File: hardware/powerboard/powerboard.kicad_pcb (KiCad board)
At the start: 2 copper layers, 45 x 30 mm, 45 parts, among them J1 BAT JST-PH 2P, J2 SERVO L, J3 SERVO R, J4 DISPLAY GC9A01, Q1 AO3401A, Q2 FS8205A, Q3 AO3401A, Q4 2N7002, Q5 AO3401A, SW1 EIN/AUS, U1 TP4054, U2 DW01A, U3 LM66100, U4 ESP32-C6-Zero

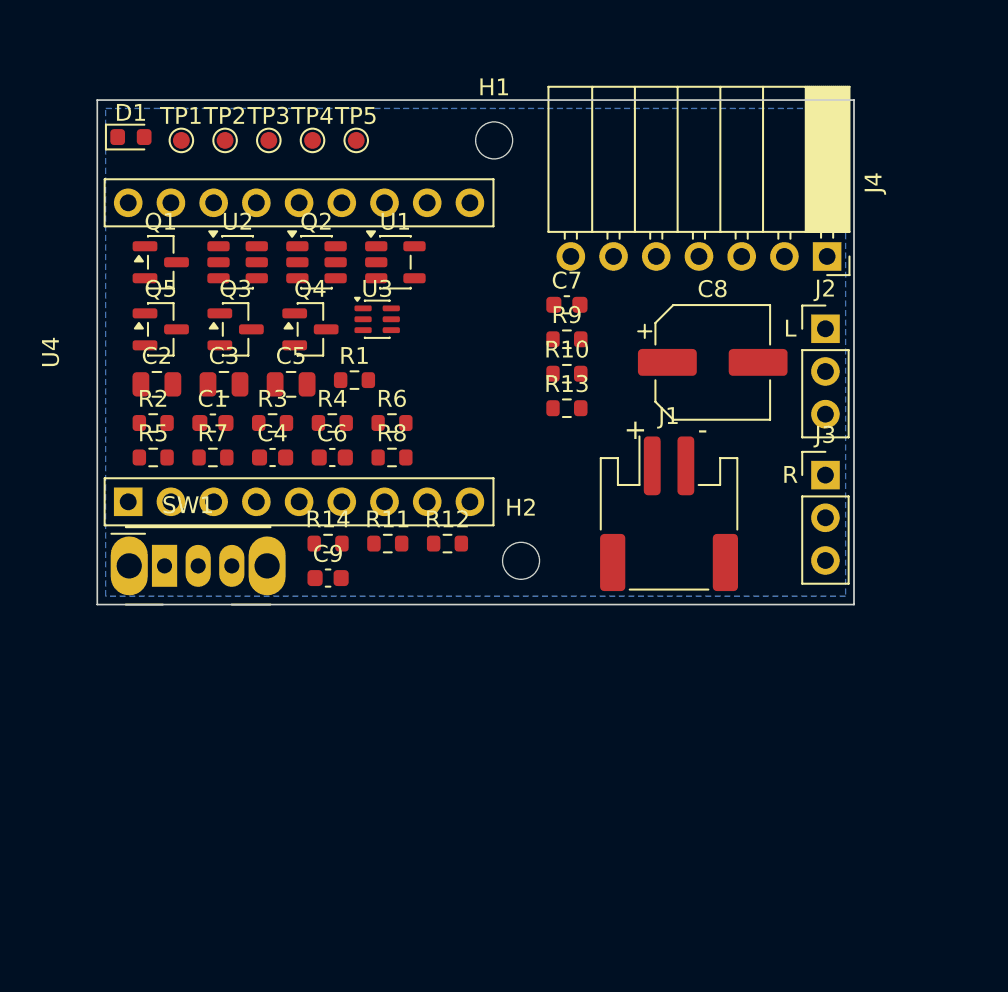
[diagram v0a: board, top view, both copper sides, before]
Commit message: Route the powerboard Rev 0.2 and add the files for a JLCPCB order
The board now has four 5 V servo ports through a TPS61023 boost, current
and voltage measurement with an INA226 on a Kelvin shunt, three analog and
two I2C ports, a THT cell connector and the outline of the shell. JLC basic
parts are used where they cost nothing in function.

The high current path (cell, reverse polarity FETs, shunt, boost, 5 V rail)
sits in one block at the front and is drawn with fixed, wide copper; the
autorouter only does signals and low current. Freerouting cannot reach pads
of parts at odd angles or next to slanted edges, so route.py rewrites the
DSN for it, tries several variants and keeps the best; maze.py closes what
is left. Labels on both sides and the KidsLab logo on the bottom.

Co-Authored-By: Claude Opus 5.5 <noreply@anthropic.com>
Claude-Session: https://claude.ai/code/session_01UqX4DjfVzW8YQJ4gc8FRQe
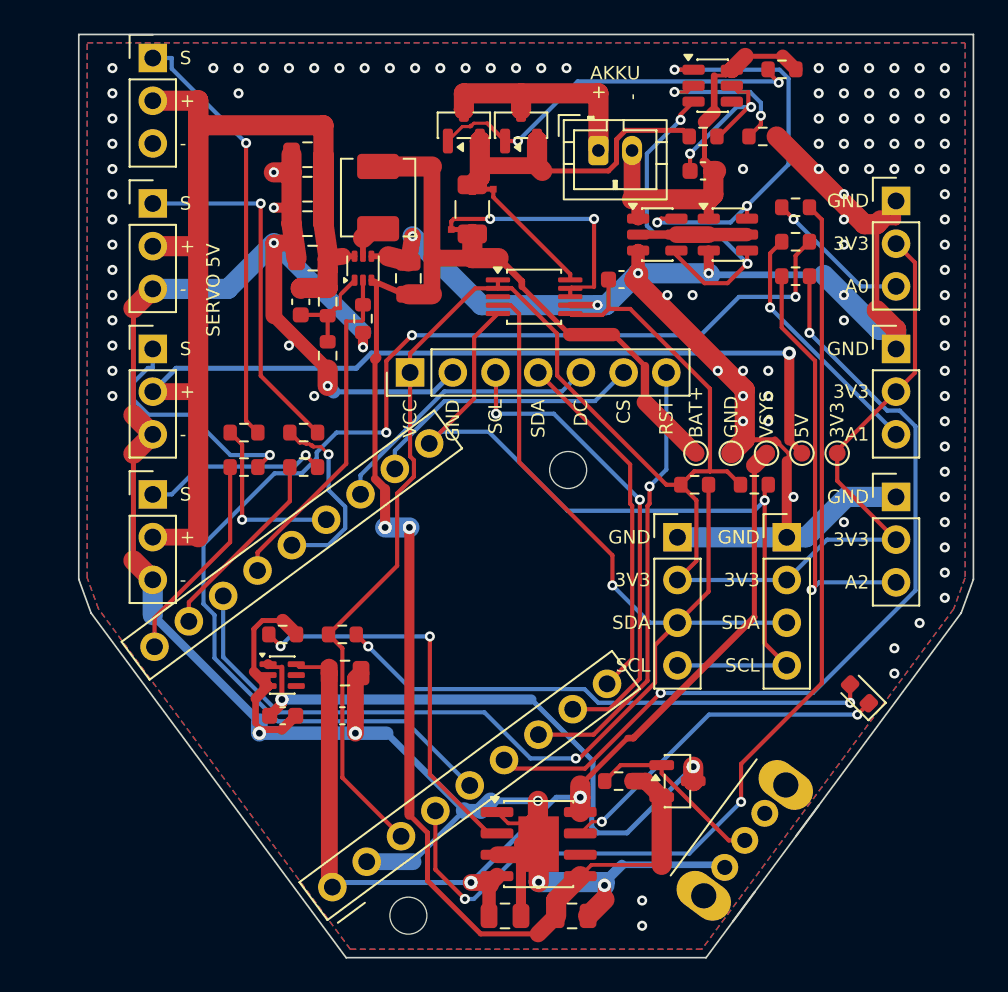
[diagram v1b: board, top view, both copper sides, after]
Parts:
- removed C8: 470u 10V, CP_Elec_6.3x7.7
- removed C9: 100n, C_0603_1608Metric
- removed Q3: AO3401A, SOT-23
- removed Q4: 2N7002, SOT-23
- removed R11, R12: 470k, R_0603_1608Metric
- removed R6: 10k, R_0603_1608Metric
- added C10: 22u, C_0805_2012Metric, F.Cu at (118.5, 110.6)
- added C11: 22u, C_0805_2012Metric, F.Cu at (112.8, 109.4)
- added C12: 22u, C_0805_2012Metric, F.Cu at (112.5, 107.3)
- added C13: 22u, C_0805_2012Metric, F.Cu at (112.5, 105.3)
- added C14: 22u, C_0805_2012Metric, F.Cu at (112.5, 103.2)
- added C15: 100n, C_0603_1608Metric, F.Cu at (131.2, 110.7)
- added J10: I2C 1, PinHeader_1x04_P2.54mm_Vertical, F.Cu at (134.5, 126.0)
- added J11: I2C 2, PinHeader_1x04_P2.54mm_Vertical, F.Cu at (141.0, 126.0)
- added J5: SERVO 3, PinHeader_1x03_P2.54mm_Vertical, F.Cu at (103.3, 114.8)
- added J6: SERVO 4, PinHeader_1x03_P2.54mm_Vertical, F.Cu at (103.3, 123.5)
- added J7: ANALOG A0, PinHeader_1x03_P2.54mm_Vertical, F.Cu at (147.5, 106.0)
- added J8: ANALOG A1, PinHeader_1x03_P2.54mm_Vertical, F.Cu at (147.5, 114.8)
- added J9: ANALOG A2, PinHeader_1x03_P2.54mm_Vertical, F.Cu at (147.5, 123.6)
- added L1: 1u, L_Sunlord_MWSA0402S, F.Cu at (116.7, 105.8)
- added LOGO1: KidsLab_Logo, KidsLab_Logo, B.Cu at (118.5, 105.5)
- added Q6: FS8205A, SOT-23-6, F.Cu at (137.5, 108.0)
- added Q7: AO3401A, SOT-23, F.Cu at (125.2, 101.5)
- added R15: 10m, R_1206_3216Metric_Kelvin, F.Cu at (122.3, 106.5)
- added R16: 220, R_0603_1608Metric, F.Cu at (108.7, 121.8)
- added R17: 220, R_0603_1608Metric, F.Cu at (112.3, 121.8)
- added R18: 1k, R_0603_1608Metric, F.Cu at (141.5, 106.4)
- added R19: 1k, R_0603_1608Metric, F.Cu at (141.5, 108.4)
- added R20: 1k, R_0603_1608Metric, F.Cu at (141.5, 110.5)
- added R21: 4.7k, R_0603_1608Metric, F.Cu at (135.5, 122.9)
- added R22: 4.7k, R_0603_1608Metric, F.Cu at (139.1, 122.9)
- added U5: INA226, TSSOP-10_3x3mm_P0.5mm, F.Cu at (126.0, 111.7)
- added U6: TPS61023, SOT-563, F.Cu at (115.8, 110.0)
- C7: value 47n -> 220p
- J1: footprint JST_PH_S2B-PH-SM4-TB_1x02-1MP_P2.00mm_Horizontal -> JST_PH_B2B-PH-K_1x02_P2.00mm_Vertical
- J2: value SERVO L -> SERVO 1
- J3: value SERVO R -> SERVO 2
- J4: footprint PinSocket_1x07_P2.54mm_Horizontal -> PinHeader_1x07_P2.54mm_Vertical
- R8: value 100k -> 750k
- R9: value 10k -> 100k
- SW1: footprint SW_Slide_SPDT_Angled_CK_OS102011MA1Q -> SW_Slide_SPDT_Angled_CK_OS102011MA1Q_Round
- TP4: value TP_VSERVO -> TP_V5_SERVO
- U1: value TP4054 -> TP4056; footprint SOT-23-5 -> SOIC-8-1EP_3.9x4.9mm_P1.27mm_EP2.41x3.3mm
- moved D1 54.5 mm to (145.3, 135.3), turned to 135 degrees
- moved J3 43.1 mm to (103.3, 106.2)
- moved J2 43.1 mm to (103.3, 97.5)
- moved Q5 40.8 mm to (134.5, 140.5)
- moved SW1 37.8 mm to (137.3, 145.6), turned to 53.4986 degrees
- moved C2 37.8 mm to (124.2, 148.5)
- moved C3 37.8 mm to (128.2, 148.5)
- moved R2 36.9 mm to (136.0, 102.2)
- moved TP1 35.8 mm to (135.6, 121.0)
- moved U1 35.6 mm to (126.2, 144.2)
- moved TP2 35.4 mm to (137.7, 121.0)
- moved TP3 35.0 mm to (139.8, 121.0)
- moved TP4 34.5 mm to (141.9, 121.0)
- moved TP5 34.1 mm to (144.0, 121.0)
- moved R3 33.8 mm to (139.6, 102.2)
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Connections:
- net /SERVO_L renamed /SERVO1
- net /SERVO_L_S renamed /SERVO1_S
- net /SERVO_R renamed /SERVO2
- net /SERVO_R_S renamed /SERVO2_S
- C7 pad 1: /SERVO_G -> /V5_SERVO
- C7 pad 2: /BAT+ -> /BOOST_FB
- J2 pad 2: /VSERVO -> /V5_SERVO
- J3 pad 2: /VSERVO -> /V5_SERVO
- Q1 pad 2: /BAT+ -> /BAT_CELL
- R2 pad 1: /BAT+ -> /BAT_CELL
- R8 pad 1: /SERVO_G -> /V5_SERVO
- R8 pad 2: /BAT+ -> /BOOST_FB
- R9 pad 1: /SERVO_G -> /BOOST_FB
- R9 pad 2: /Q4_D -> /GND
- TP4 pad 1: /VSERVO -> /V5_SERVO
- U1 pad 1: /CHRG_N -> /GND
- U1 pad 2: /GND -> /PROG
- U1 pad 3: /BAT+ -> /GND
- U1 pad 5: /PROG -> /BAT+
- U4 pad 10: (no net) -> /SERVO3
- U4 pad 11: (no net) -> /SERVO4
- U4 pad 12: (no net) -> /I2C_SDA
- U4 pad 13: (no net) -> /SERVO_EN
- U4 pad 18: (no net) -> /I2C_SCL
- U4 pad 4: /VBAT_SENSE -> /A0_IO
- U4 pad 5: /CHRG_IO -> /A1_IO
- U4 pad 6: /SERVO_EN -> /A2_IO
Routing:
- net /GND: track 0.00 -> 243.8 mm, vias 0 -> 115
- net /3V3: track 0.00 -> 120.5 mm
- net /V5_SERVO: track 0.00 -> 115.0 mm, vias 0 -> 1
- net /BAT+: track 0.00 -> 99.0 mm, vias 0 -> 2
- net /I2C_SDA: track 0.00 -> 78.0 mm, vias 0 -> 2
- net /A1_IO: track 0.00 -> 73.0 mm, vias 0 -> 3
- net /A0_IO: track 0.00 -> 62.4 mm, vias 0 -> 2
- net /VSYS: track 0.00 -> 61.9 mm, vias 0 -> 2
- net /A2_IO: track 0.00 -> 50.8 mm, vias 0 -> 2
- net /I2C_SCL: track 0.00 -> 49.7 mm, vias 0 -> 1
- net /BAT_SW: track 0.00 -> 36.7 mm, vias 0 -> 2
- net /LED_A: track 0.00 -> 32.1 mm, vias 0 -> 2
- net /TFT_SCK: track 0.00 -> 28.5 mm, vias 0 -> 2
- net /TFT_RST: track 0.00 -> 26.6 mm, vias 0 -> 1
- net /SERVO1_S: track 0.00 -> 25.5 mm, vias 0 -> 1
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- added copper zone on F.Cu, net /GND
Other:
- board size 45 x 30 mm -> 53.2 x 54.9 mm
- board text added: "3V3"
- board text added: "5V"
- board text added: "A0"
- board text added: "A1"
- board text added: "A2"
- board text added: "AKKU"
- board text added: "ANALOG A0"
- board text added: "ANALOG A1"
- board text added: "ANALOG A2"
- board text added: "BAT+"
- board text added: "CS"
- board text added: "DC"
- board text added: "DISPLAY"
- board text added: "EIN/AUS"
- board text added: "GND"
- board text added: "I2C 1"
- board text added: "I2C 2"
- board text added: "LADE-LED"
- board text added: "MF26 v0.2"
- board text added: "RST"
- board text added: "Robo-Buddy Power"
- board text added: "S"
- board text added: "SCL"
- board text added: "SDA"
- board text added: "SERVO 1"
- board text added: "SERVO 2"
- board text added: "SERVO 3"
- board text added: "SERVO 4"
- board text added: "SERVO 5V"
- board text added: "VCC"
- board text added: "VSYS"
- board text removed: "KidsLab - VORLAEUFIG, nicht bestellen"
- board text removed: "L"
- board text removed: "MF26 Robo-Buddy Power v0.1"
- board text removed: "R"

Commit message: Use the 15.24 mm pin row spacing of the ESP32-C6-Zero from Waveshare's DXF
The footprint assumed 17.78 mm with half pads at the edge; the DXF says
15.24 mm, with the holes 1.38 mm in from the board edge. The keepout under
the antenna now follows the row spacing so it stays clear of the pins.
Board rerouted, views and JLCPCB files regenerated; the BOM rows are now
sorted in a fixed order.

Co-Authored-By: Claude Opus 5.5 <noreply@anthropic.com>
Claude-Session: https://claude.ai/code/session_01UqX4DjfVzW8YQJ4gc8FRQe
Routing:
- net /VSYS: track 61.9 -> 83.8 mm, vias 2 -> 1
- net /A1_IO: track 73.0 -> 54.3 mm, vias 3 -> 1
- net /3V3: track 120.5 -> 105.3 mm
- net /A2_IO: track 50.8 -> 40.5 mm, vias 2 -> 1
- net /I2C_SDA: track 78.0 -> 69.4 mm
- net /V5_SERVO: track 115.0 -> 106.4 mm
- net /GND: track 243.8 -> 250.7 mm, vias 115 -> 107
- net /SENSE_N: track 15.0 -> 9.79 mm, vias 2 -> 0
- net /SERVO3_S: track 14.1 -> 9.82 mm
- net /SERVO1_S: track 25.5 -> 29.6 mm
- net /TFT_SCK: track 28.5 -> 25.0 mm, vias 2 -> 0
- net /DW_VDD: track 10.6 -> 7.33 mm, vias 2 -> 0
- net /SERVO1: track 10.5 -> 13.7 mm
- net /BAT_SW: track 36.7 -> 33.8 mm, vias 2 -> 4
- net /SW_GATE: track 10.9 -> 13.5 mm
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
